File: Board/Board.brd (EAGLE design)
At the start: 54.2 x 85.1 mm, 65 parts, among them IC1 MEGA8-AI, IC2 LM358D, IC4 MCP3426, IC6 MCP4921, IC7 TL431CD, Q1 IRLIZ44N, T1 BC817, U1 CJT1117-3.3-SOT223, U3 MCP9701AT-E/TT, U4 IRLML2502

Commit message: firmware improvements
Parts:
- IC1: value MEGA8-AI -> MEGA328
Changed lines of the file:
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@@
 <attribute name="VALUE" x="42.555" y="37.69" size="0.889" layer="28" ratio="11" rot="MR90"/>
 </element>
-<element name="IC1" library="atmel" library_urn="urn:adsk.eagle:library:105" package="TQFP32-08" package3d_urn="urn:adsk.eagle:package:4313/1" value="MEGA8-AI" x="17" y="13" smashed="yes" rot="MR225">
+<element name="IC1" library="atmel" library_urn="urn:adsk.eagle:library:105" package="TQFP32-08" package3d_urn="urn:adsk.eagle:package:4313/1" value="MEGA328" x="17" y="13" smashed="yes" rot="MR225">
 <attribute name="MF" value="" x="17" y="13" size="1.778" layer="28" rot="MR225" display="off"/>
 <attribute name="MPN" value="ATMEGA8-16AU" x="17" y="13" size="1.778" layer="28" rot="MR225" display="off"/>

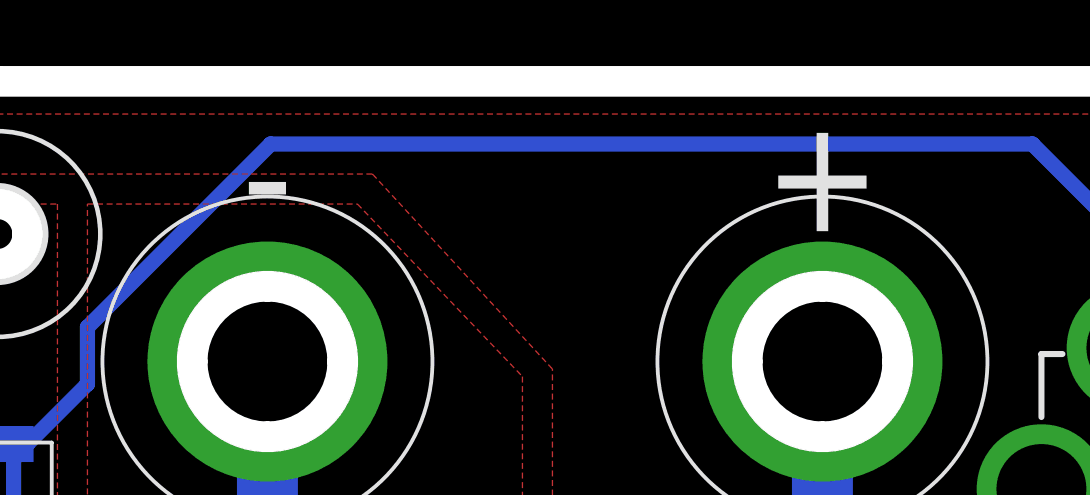
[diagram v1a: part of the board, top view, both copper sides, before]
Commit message: added nupo logo to bottom silkscreen
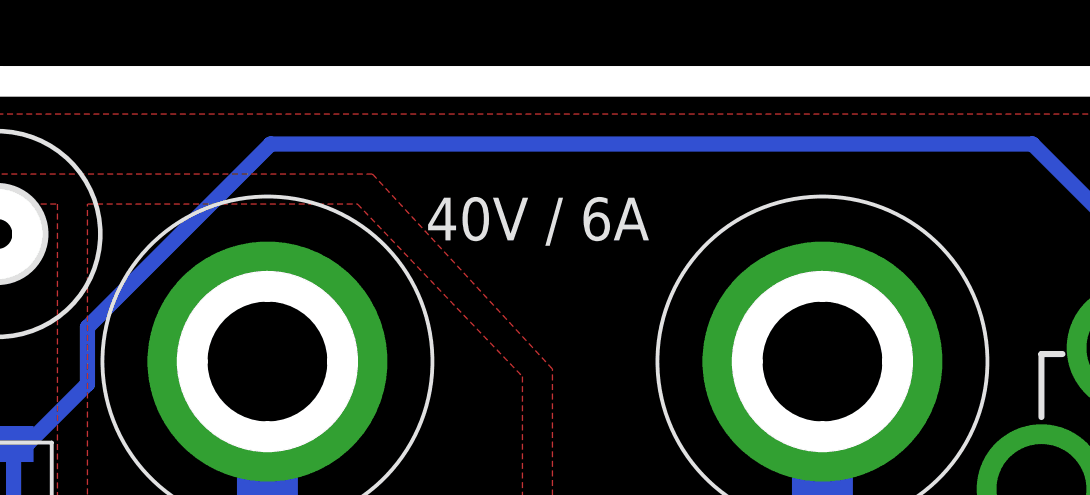
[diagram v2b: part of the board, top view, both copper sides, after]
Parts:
- added U$1: (no value), OwnStuff:LOGO-SILKSCREEEN-S
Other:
- board text added: "40V / 6A"
- board text added: "PocketLoad by nupo-artworks.de"
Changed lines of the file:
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@@
 <wire x1="48" y1="-1" x2="4" y2="-1" width="1" layer="46"/>
 <wire x1="4" y1="-1" x2="-1.1" y2="4" width="1" layer="46" curve="-90"/>
-<text x="31.5" y="81" size="3.81" layer="21" align="center">+</text>
-<text x="13" y="81" size="3.81" layer="21" align="center">-</text>
 <wire x1="4" y1="78" x2="3" y2="79" width="1" layer="46" curve="-90"/>
 <wire x1="3" y1="79" x2="4" y2="80" width="1" layer="46" curve="-90"/>
@@
 <wire x1="31.5" y1="77.25" x2="34" y2="74.75" width="1" layer="46" curve="-90"/>
 <wire x1="34" y1="74.75" x2="31.5" y2="72.25" width="1" layer="46" curve="-90"/>
+<text x="41.5" y="29" size="0.6096" layer="22" rot="MR0" align="center">PocketLoad
+by nupo-artworks.de</text>
+<text x="22" y="79.5" size="1.4224" layer="21" align="center">40V / 6A</text>
 </plain>
 <attributes>
@@
 <attribute name="VALUE" x="11.635" y="5.595" size="1.27" layer="28" rot="MR0"/>
 </element>
+<element name="U$1" library="OwnStuff" package="LOGO-SILKSCREEEN-S" value="" x="41.5" y="31" rot="MR0"/>
 </elements>
 <signals>

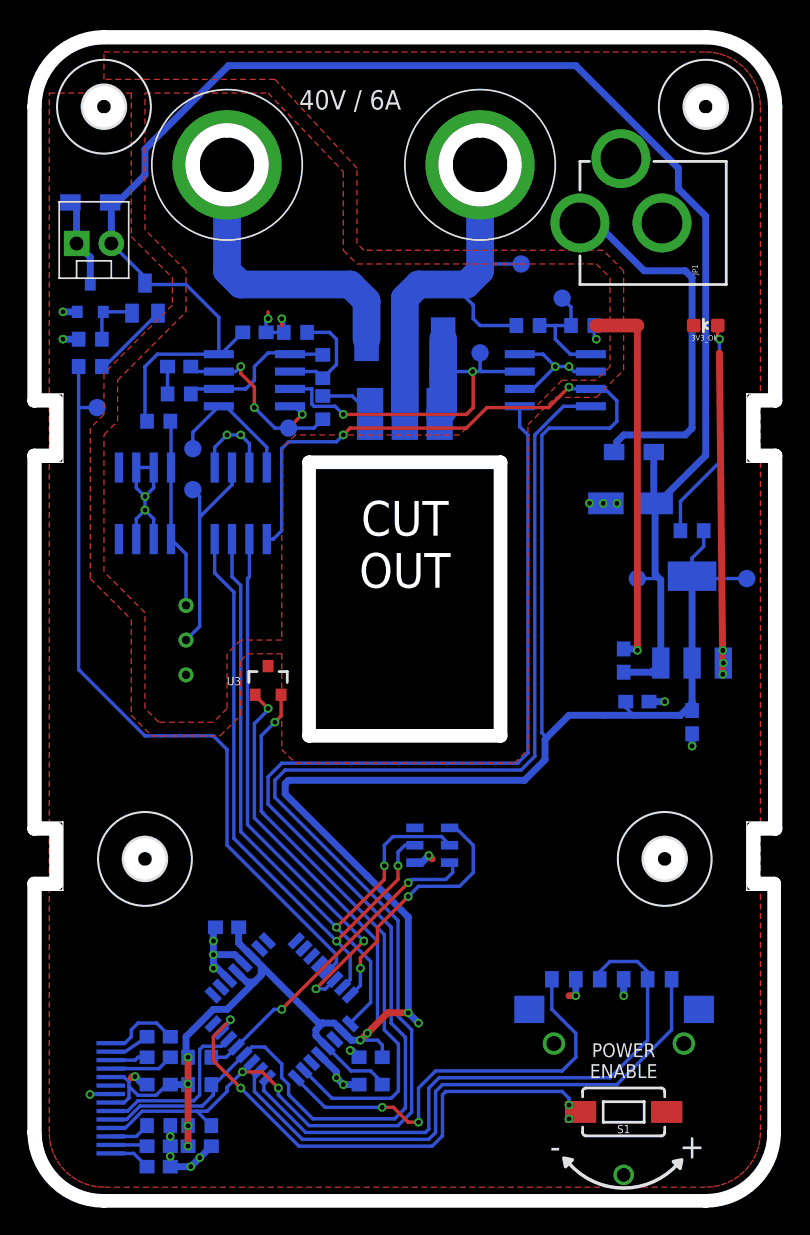
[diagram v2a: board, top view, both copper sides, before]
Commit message: added OSHW logo
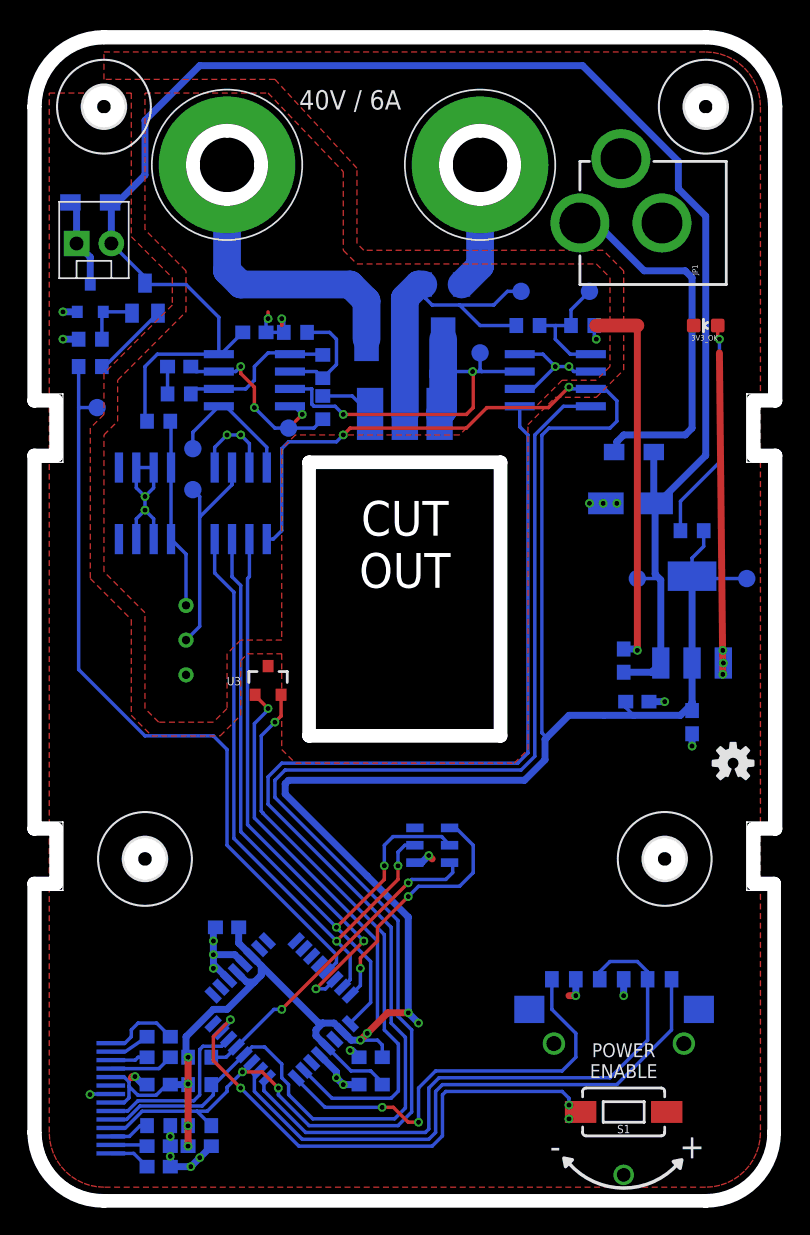
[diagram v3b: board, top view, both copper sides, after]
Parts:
- removed VLOAD, VLOAD_ATT: TPB1,27, testpad:B1,27
- added F1: 6.3A/63V, Seeed-OPL-fuse:F1206
- added U$3: (no value), SparkFun-Aesthetics:OSHW-LOGO-S
- added UATT, ULOAD: TPB1,27, testpad:B1,27
- renumbered FET_DRV to UDRV, VLOAD_DROP to UDROP, VLOAD_REF to USET
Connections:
- new net N$7: F1.1, IN+.P$1
- net LOAD+: now also F1.2, ULOAD.TP; no longer IN+.P$1, VLOAD.TP
- net VLOAD_ATT: now also UATT.TP; no longer VLOAD_ATT.TP
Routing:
- net N$7: track 0.00 -> 9.31 mm
- net LOAD+: track 32.2 -> 23.7 mm
- net +12V: track 125.6 -> 127.1 mm
- net VLOAD_ATT: track 8.79 -> 9.58 mm

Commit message: added link to github repo
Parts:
- moved U$3 17.1 mm to (36.5, 20.5), flipped to the bottom
- moved U$1 15.2 mm to (31.0, 20.0)
- moved C10 0.52 mm to (11.1, 2.50)
- moved R11 0.52 mm to (11.1, 4.00)
- moved C14 0.50 mm to (8.00, 1.00)
- moved C15 0.50 mm to (8.00, 2.50)
- moved R10 0.50 mm to (8.00, 4.00)
- moved R9 0.18 mm to (11.1, 9.38)
- moved C12 0.12 mm to (8.00, 9.38)
- moved C13 0.12 mm to (8.00, 10.9)
- moved R14 0.12 mm to (11.1, 7.50)
- moved R8 0.12 mm to (20.0, 60.1)
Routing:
- net GND: track 139.2 -> 115.0 mm
- net SCK: track 53.3 -> 56.3 mm
- net +3V3: track 222.7 -> 224.3 mm
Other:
- board size 54.2 x 85.1 mm -> 53.2 x 84.2 mm
- board text added: "github.com/dangrie158/pocket-load"

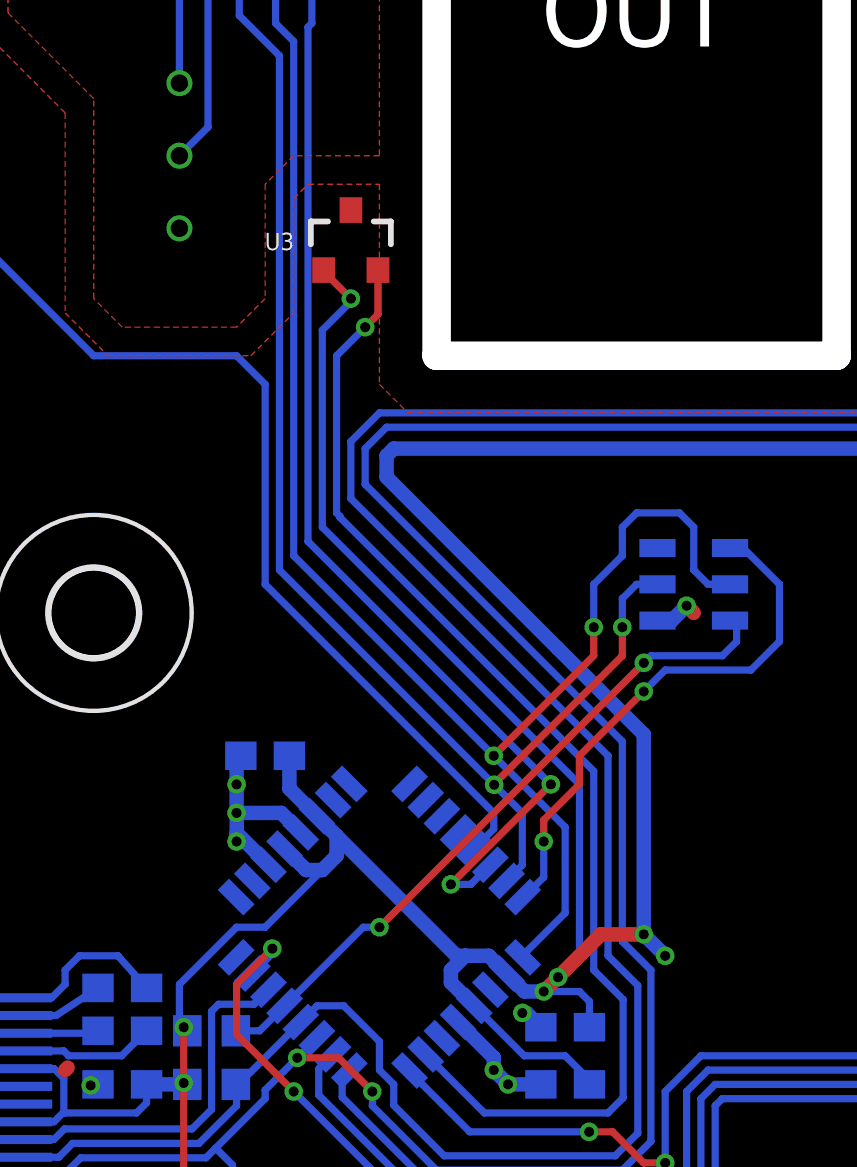
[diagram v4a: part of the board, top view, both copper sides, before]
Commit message: improved thermal performance of temp sensor
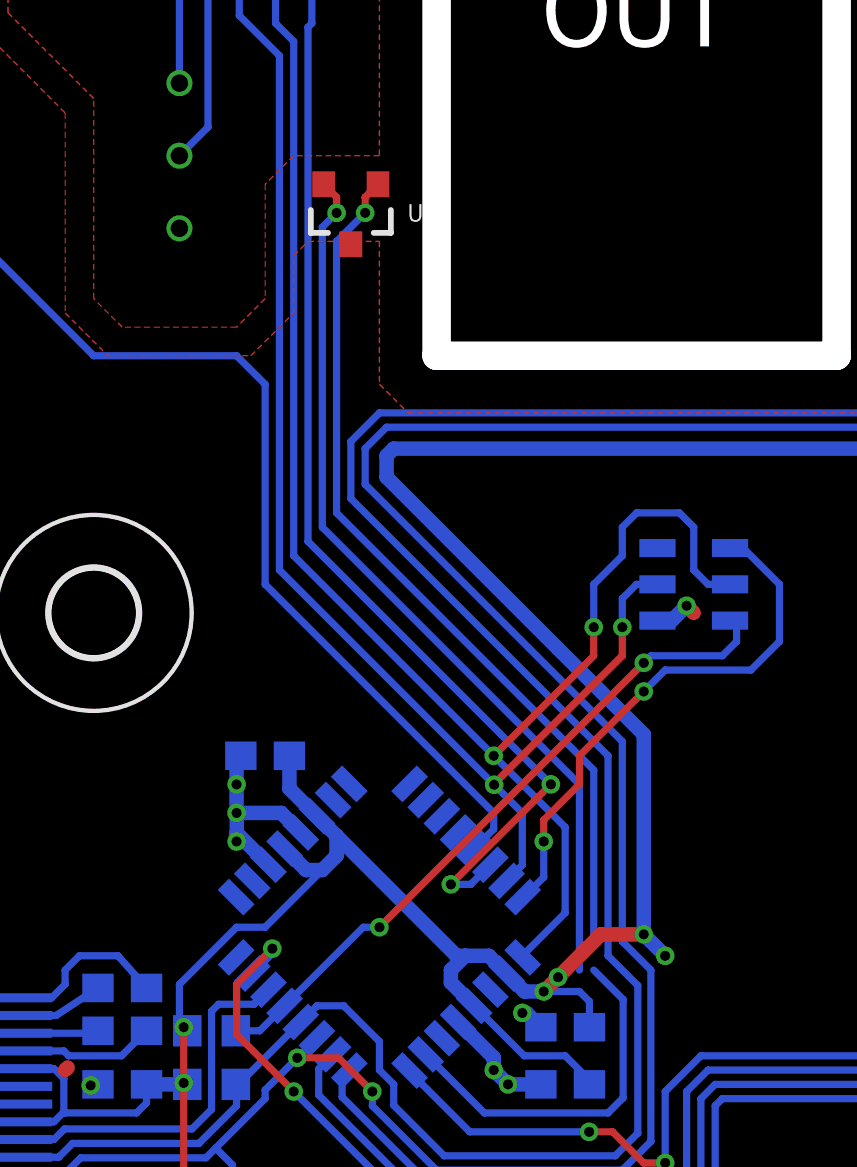
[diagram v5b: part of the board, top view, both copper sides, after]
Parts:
- moved U3 1.00 mm to (16.0, 38.0), turned to 180 degrees
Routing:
- net TEMP: track 41.7 -> 44.5 mm
- net +3V3: track 224.3 -> 225.6 mm
